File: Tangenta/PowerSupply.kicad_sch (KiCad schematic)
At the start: 64 parts, among them J1 39281243, U1 TPS54331DR, U2 TPS54331DR, U3 TPS54331DR, U4 TPS54331DR, U5 AMS1117-3_3, U6 AP7331-10WG-7

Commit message: AMS1117-3.3 and AP7331-10WG-7
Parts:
- U6: footprint AP7331-10WG:AP7331-10WG.kicad_sym -> CholaFootprintsPrjLib:AP7331-10WG.kicad_sym
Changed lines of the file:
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@@
       (effects (font (size 1.27 1.27)))
     )
-    (property "Footprint" "AP7331-10WG:AP7331-10WG.kicad_sym" (at 244.475 77.47 0)
+    (property "Footprint" "CholaFootprintsPrjLib:AP7331-10WG.kicad_sym" (at 244.475 77.47 0)
       (effects (font (size 1.27 1.27) italic) hide)
     )

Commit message: 24_Pin_Connector_Vertical
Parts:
- J1: footprint 24_Pin_Connector_Vertical:24_Pin_Connector_Vertical -> CholaFootprintsPrjLib:24_Pin_Connector_Vertical
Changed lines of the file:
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@@
       (effects (font (size 1.27 1.27)))
     )
-    (property "Footprint" "24_Pin_Connector_Vertical:24_Pin_Connector_Vertical" (at 191.135 158.496 0)
+    (property "Footprint" "CholaFootprintsPrjLib:24_Pin_Connector_Vertical" (at 191.135 158.496 0)
       (effects (font (size 1.27 1.27) italic) hide)
     )

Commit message: TPS54331DR
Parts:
- U1, U2, U3, U4: footprint TPS54331DR:TPS54331DR -> CholaFootprintsPrjLib:TPS54331DR
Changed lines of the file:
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@@
     )
   )
-  (symbol (lib_id "CholaSymbolsPrjLib:TPS54331DR") (at 85.725 71.12 0) (unit 1)
+  (symbol (lib_name "TPS54331DR_2") (lib_id "CholaSymbolsPrjLib:TPS54331DR") (at 85.725 71.12 0) (unit 1)
     (in_bom yes) (on_board yes) (dnp no) (fields_autoplaced)
     (property "Reference" "U2" (at 85.725 55.88 0)
@@
       (effects (font (size 1.27 1.27)))
     )
-    (property "Footprint" "TPS54331DR:TPS54331DR" (at 85.725 81.28 0)
+    (property "Footprint" "CholaFootprintsPrjLib:TPS54331DR" (at 85.725 81.28 0)
       (effects (font (size 1.27 1.27) italic) hide)
     )
@@
     )
   )
-  (symbol (lib_id "CholaSymbolsPrjLib:TPS54331DR") (at 85.725 111.125 0) (unit 1)
+  (symbol (lib_name "TPS54331DR_3") (lib_id "CholaSymbolsPrjLib:TPS54331DR") (at 85.725 111.125 0) (unit 1)
     (in_bom yes) (on_board yes) (dnp no) (fields_autoplaced)
     (property "Reference" "U3" (at 85.725 95.885 0)
@@
       (effects (font (size 1.27 1.27)))
     )
-    (property "Footprint" "TPS54331DR:TPS54331DR" (at 85.725 121.285 0)
+    (property "Footprint" "CholaFootprintsPrjLib:TPS54331DR" (at 85.725 121.285 0)
       (effects (font (size 1.27 1.27) italic) hide)
     )
@@
       (effects (font (size 1.27 1.27)))
     )
-    (property "Footprint" "TPS54331DR:TPS54331DR" (at 85.725 161.925 0)
+    (property "Footprint" "CholaFootprintsPrjLib:TPS54331DR" (at 85.725 161.925 0)
       (effects (font (size 1.27 1.27) italic) hide)
     )
@@
     )
   )
-  (symbol (lib_id "CholaSymbolsPrjLib:TPS54331DR") (at 85.725 31.75 0) (unit 1)
+  (symbol (lib_name "TPS54331DR_1") (lib_id "CholaSymbolsPrjLib:TPS54331DR") (at 85.725 31.75 0) (unit 1)
     (in_bom yes) (on_board yes) (dnp no) (fields_autoplaced)
     (property "Reference" "U1" (at 85.725 16.51 0)
@@
       (effects (font (size 1.27 1.27)))
     )
-    (property "Footprint" "TPS54331DR:TPS54331DR" (at 85.725 41.91 0)
-      (effects (font (size 1.27 1.27) italic) hide)
-    )
+    (property "Footprint" "CholaFootprintsPrjLib:TPS54331DR" (at 85.725 41.91 0)
+      (effects (font (size 1.27 1.27) italic) hide)
+    )

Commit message: B540C-13-F, CAP_L6
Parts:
- C2, C22, C23, C24, C25, C3, C4, C5: footprint CAP_L6:CAP_L6 -> CholaFootprintsPrjLib:CAP_L6
- D1, D2, D3, D4: footprint B540C-13-F:B540C-13-F -> CholaFootprintsPrjLib:B540C-13-F
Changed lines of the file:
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@@
       (effects (font (size 1.27 1.27)) (justify left))
     )
-    (property "Footprint" "CAP_L6:CAP_L6" (at 33.528 48.26 0)
+    (property "Footprint" "CholaFootprintsPrjLib:CAP_L6" (at 33.528 48.26 0)
       (effects (font (size 1.27 1.27) italic) hide)
     )
@@
     )
   )
-  (symbol (lib_id "CholaSymbolsPrjLib:35CE47AX") (at 30.48 108.585 0) (unit 1)
+  (symbol (lib_name "35CE47AX_6") (lib_id "CholaSymbolsPrjLib:35CE47AX") (at 30.48 108.585 0) (unit 1)
     (in_bom yes) (on_board yes) (dnp no)
     (property "Reference" "C4" (at 32.385 107.95 0)
@@
       (effects (font (size 1.27 1.27)) (justify left))
     )
-    (property "Footprint" "CAP_L6:CAP_L6" (at 33.528 127.635 0)
+    (property "Footprint" "CholaFootprintsPrjLib:CAP_L6" (at 33.528 127.635 0)
       (effects (font (size 1.27 1.27) italic) hide)
     )
@@
     )
   )
-  (symbol (lib_id "CholaSymbolsPrjLib:35CE47AX") (at 143.51 113.665 0) (unit 1)
+  (symbol (lib_name "35CE47AX_3") (lib_id "CholaSymbolsPrjLib:35CE47AX") (at 143.51 113.665 0) (unit 1)
     (in_bom yes) (on_board yes) (dnp no)
     (property "Reference" "C24" (at 145.415 113.665 0)
@@
       (effects (font (size 1.27 1.27)) (justify left))
     )
-    (property "Footprint" "CAP_L6:CAP_L6" (at 146.558 132.715 0)
+    (property "Footprint" "CholaFootprintsPrjLib:CAP_L6" (at 146.558 132.715 0)
       (effects (font (size 1.27 1.27) italic) hide)
     )
@@
     )
   )
-  (symbol (lib_id "CholaSymbolsPrjLib:B540C-13-F") (at 117.475 108.585 0) (unit 1)
+  (symbol (lib_name "B540C-13-F_3") (lib_id "CholaSymbolsPrjLib:B540C-13-F") (at 117.475 108.585 0) (unit 1)
     (in_bom yes) (on_board yes) (dnp no)
     (property "Reference" "D3" (at 116.205 106.045 0)
@@
       (effects (font (size 1.27 1.27)) (justify left) hide)
     )
-    (property "Footprint" "B540C-13-F:B540C-13-F" (at 117.602 120.142 0)
+    (property "Footprint" "CholaFootprintsPrjLib:B540C-13-F" (at 117.602 120.142 0)
       (effects (font (size 1.27 1.27) italic) hide)
     )
@@
     )
   )
-  (symbol (lib_id "CholaSymbolsPrjLib:35CE47AX") (at 30.48 149.225 0) (unit 1)
+  (symbol (lib_name "35CE47AX_5") (lib_id "CholaSymbolsPrjLib:35CE47AX") (at 30.48 149.225 0) (unit 1)
     (in_bom yes) (on_board yes) (dnp no)
     (property "Reference" "C5" (at 32.385 148.59 0)
@@
       (effects (font (size 1.27 1.27)) (justify left))
     )
-    (property "Footprint" "CAP_L6:CAP_L6" (at 33.528 168.275 0)
+    (property "Footprint" "CholaFootprintsPrjLib:CAP_L6" (at 33.528 168.275 0)
       (effects (font (size 1.27 1.27) italic) hide)
     )
@@
     )
   )
-  (symbol (lib_id "CholaSymbolsPrjLib:35CE47AX") (at 143.51 154.305 0) (unit 1)
+  (symbol (lib_name "35CE47AX_4") (lib_id "CholaSymbolsPrjLib:35CE47AX") (at 143.51 154.305 0) (unit 1)
     (in_bom yes) (on_board yes) (dnp no)
     (property "Reference" "C25" (at 145.415 154.305 0)
@@
       (effects (font (size 1.27 1.27)) (justify left))
     )
-    (property "Footprint" "CAP_L6:CAP_L6" (at 146.558 173.355 0)
+    (property "Footprint" "CholaFootprintsPrjLib:CAP_L6" (at 146.558 173.355 0)
       (effects (font (size 1.27 1.27) italic) hide)
     )
@@
     )
   )
-  (symbol (lib_id "CholaSymbolsPrjLib:B540C-13-F") (at 117.475 68.58 0) (unit 1)
+  (symbol (lib_name "B540C-13-F_2") (lib_id "CholaSymbolsPrjLib:B540C-13-F") (at 117.475 68.58 0) (unit 1)
     (in_bom yes) (on_board yes) (dnp no)
     (property "Reference" "D2" (at 116.205 66.04 0)
@@
       (effects (font (size 1.27 1.27)) (justify left) hide)
     )
-    (property "Footprint" "B540C-13-F:B540C-13-F" (at 117.602 80.137 0)
+    (property "Footprint" "CholaFootprintsPrjLib:B540C-13-F" (at 117.602 80.137 0)
       (effects (font (size 1.27 1.27) italic) hide)
     )
@@
       (effects (font (size 1.27 1.27)) (justify left) hide)
     )
-    (property "Footprint" "B540C-13-F:B540C-13-F" (at 117.602 160.782 0)
+    (property "Footprint" "CholaFootprintsPrjLib:B540C-13-F" (at 117.602 160.782 0)
       (effects (font (size 1.27 1.27) italic) hide)
     )
@@
     )
   )
-  (symbol (lib_id "CholaSymbolsPrjLib:B540C-13-F") (at 117.475 29.21 0) (unit 1)
+  (symbol (lib_name "B540C-13-F_1") (lib_id "CholaSymbolsPrjLib:B540C-13-F") (at 117.475 29.21 0) (unit 1)
     (in_bom yes) (on_board yes) (dnp no)
     (property "Reference" "D1" (at 116.205 26.67 0)
@@
       (effects (font (size 1.27 1.27)) (justify left) hide)
     )
-    (property "Footprint" "B540C-13-F:B540C-13-F" (at 117.602 40.767 0)
+    (property "Footprint" "CholaFootprintsPrjLib:B540C-13-F" (at 117.602 40.767 0)
       (effects (font (size 1.27 1.27) italic) hide)
     )
@@
     )
   )
-  (symbol (lib_id "CholaSymbolsPrjLib:35CE47AX") (at 143.51 73.66 0) (unit 1)
+  (symbol (lib_name "35CE47AX_2") (lib_id "CholaSymbolsPrjLib:35CE47AX") (at 143.51 73.66 0) (unit 1)
     (in_bom yes) (on_board yes) (dnp no)
     (property "Reference" "C23" (at 145.415 73.66 0)
@@
       (effects (font (size 1.27 1.27)) (justify left))
     )
-    (property "Footprint" "CAP_L6:CAP_L6" (at 146.558 92.71 0)
+    (property "Footprint" "CholaFootprintsPrjLib:CAP_L6" (at 146.558 92.71 0)
       (effects (font (size 1.27 1.27) italic) hide)
     )
@@
     )
   )
-  (symbol (lib_id "CholaSymbolsPrjLib:35CE47AX") (at 143.51 34.29 0) (unit 1)
+  (symbol (lib_name "35CE47AX_1") (lib_id "CholaSymbolsPrjLib:35CE47AX") (at 143.51 34.29 0) (unit 1)
     (in_bom yes) (on_board yes) (dnp no)
     (property "Reference" "C22" (at 145.415 34.29 0)
@@
       (effects (font (size 1.27 1.27)) (justify left))
     )
-    (property "Footprint" "CAP_L6:CAP_L6" (at 146.558 53.34 0)
+    (property "Footprint" "CholaFootprintsPrjLib:CAP_L6" (at 146.558 53.34 0)
       (effects (font (size 1.27 1.27) italic) hide)
     )
@@
     )
   )
-  (symbol (lib_id "CholaSymbolsPrjLib:35CE47AX") (at 30.48 68.58 0) (unit 1)
+  (symbol (lib_name "35CE47AX_7") (lib_id "CholaSymbolsPrjLib:35CE47AX") (at 30.48 68.58 0) (unit 1)
     (in_bom yes) (on_board yes) (dnp no)
     (property "Reference" "C3" (at 32.385 67.945 0)
@@
       (effects (font (size 1.27 1.27)) (justify left))
     )
-    (property "Footprint" "CAP_L6:CAP_L6" (at 33.528 87.63 0)
-      (effects (font (size 1.27 1.27) italic) hide)
-    )
+    (property "Footprint" "CholaFootprintsPrjLib:CAP_L6" (at 33.528 87.63 0)
+      (effects (font (size 1.27 1.27) italic) hide)
+    )

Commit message: SLO0650H6Р8МТТ, CAP_TANTAL_A
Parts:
- C26, C27, C28, C29, C32: footprint CAP_TANTAL_A:CAP_TANTAL_A -> CholaFootprintsPrjLib:CAP_TANTAL_A
- L1, L2, L3, L4: footprint Choke:Choke -> CholaFootprintsPrjLib:Choke
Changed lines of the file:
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@@
       (effects (font (size 1.27 1.27)))
     )
-    (property "Footprint" "Choke:Choke" (at 120.015 132.334 0)
+    (property "Footprint" "CholaFootprintsPrjLib:Choke" (at 120.015 132.334 0)
       (effects (font (size 1.27 1.27) italic) hide)
     )
@@
       (effects (font (size 1.27 1.27)) (justify right))
     )
-    (property "Footprint" "CAP_TANTAL_A:CAP_TANTAL_A" (at 140.081 110.617 0)
+    (property "Footprint" "CholaFootprintsPrjLib:CAP_TANTAL_A" (at 140.081 110.617 0)
       (effects (font (size 1.27 1.27) italic) hide)
     )
@@
       (effects (font (size 1.27 1.27)) (justify right))
     )
-    (property "Footprint" "CAP_TANTAL_A:CAP_TANTAL_A" (at 140.081 31.242 0)
+    (property "Footprint" "CholaFootprintsPrjLib:CAP_TANTAL_A" (at 140.081 31.242 0)
       (effects (font (size 1.27 1.27) italic) hide)
     )
@@
       (effects (font (size 1.27 1.27)))
     )
-    (property "Footprint" "Choke:Choke" (at 120.015 12.319 0)
+    (property "Footprint" "CholaFootprintsPrjLib:Choke" (at 120.015 12.319 0)
       (effects (font (size 1.27 1.27) italic) hide)
     )
@@
       (effects (font (size 1.27 1.27)))
     )
-    (property "Footprint" "Choke:Choke" (at 120.015 51.689 0)
+    (property "Footprint" "CholaFootprintsPrjLib:Choke" (at 120.015 51.689 0)
       (effects (font (size 1.27 1.27) italic) hide)
     )
@@
       (effects (font (size 1.27 1.27)) (justify right))
     )
-    (property "Footprint" "CAP_TANTAL_A:CAP_TANTAL_A" (at 241.681 33.782 0)
+    (property "Footprint" "CholaFootprintsPrjLib:CAP_TANTAL_A" (at 241.681 33.782 0)
       (effects (font (size 1.27 1.27) italic) hide)
     )
@@
       (effects (font (size 1.27 1.27)) (justify right))
     )
-    (property "Footprint" "CAP_TANTAL_A:CAP_TANTAL_A" (at 140.081 70.612 0)
+    (property "Footprint" "CholaFootprintsPrjLib:CAP_TANTAL_A" (at 140.081 70.612 0)
       (effects (font (size 1.27 1.27) italic) hide)
     )
@@
       (effects (font (size 1.27 1.27)))
     )
-    (property "Footprint" "Choke:Choke" (at 120.015 91.694 0)
+    (property "Footprint" "CholaFootprintsPrjLib:Choke" (at 120.015 91.694 0)
       (effects (font (size 1.27 1.27) italic) hide)
     )
@@
       (effects (font (size 1.27 1.27)) (justify right))
     )
-    (property "Footprint" "CAP_TANTAL_A:CAP_TANTAL_A" (at 140.081 151.257 0)
-      (effects (font (size 1.27 1.27) italic) hide)
-    )
+    (property "Footprint" "CholaFootprintsPrjLib:CAP_TANTAL_A" (at 140.081 151.257 0)
+      (effects (font (size 1.27 1.27) italic) hide)
+    )

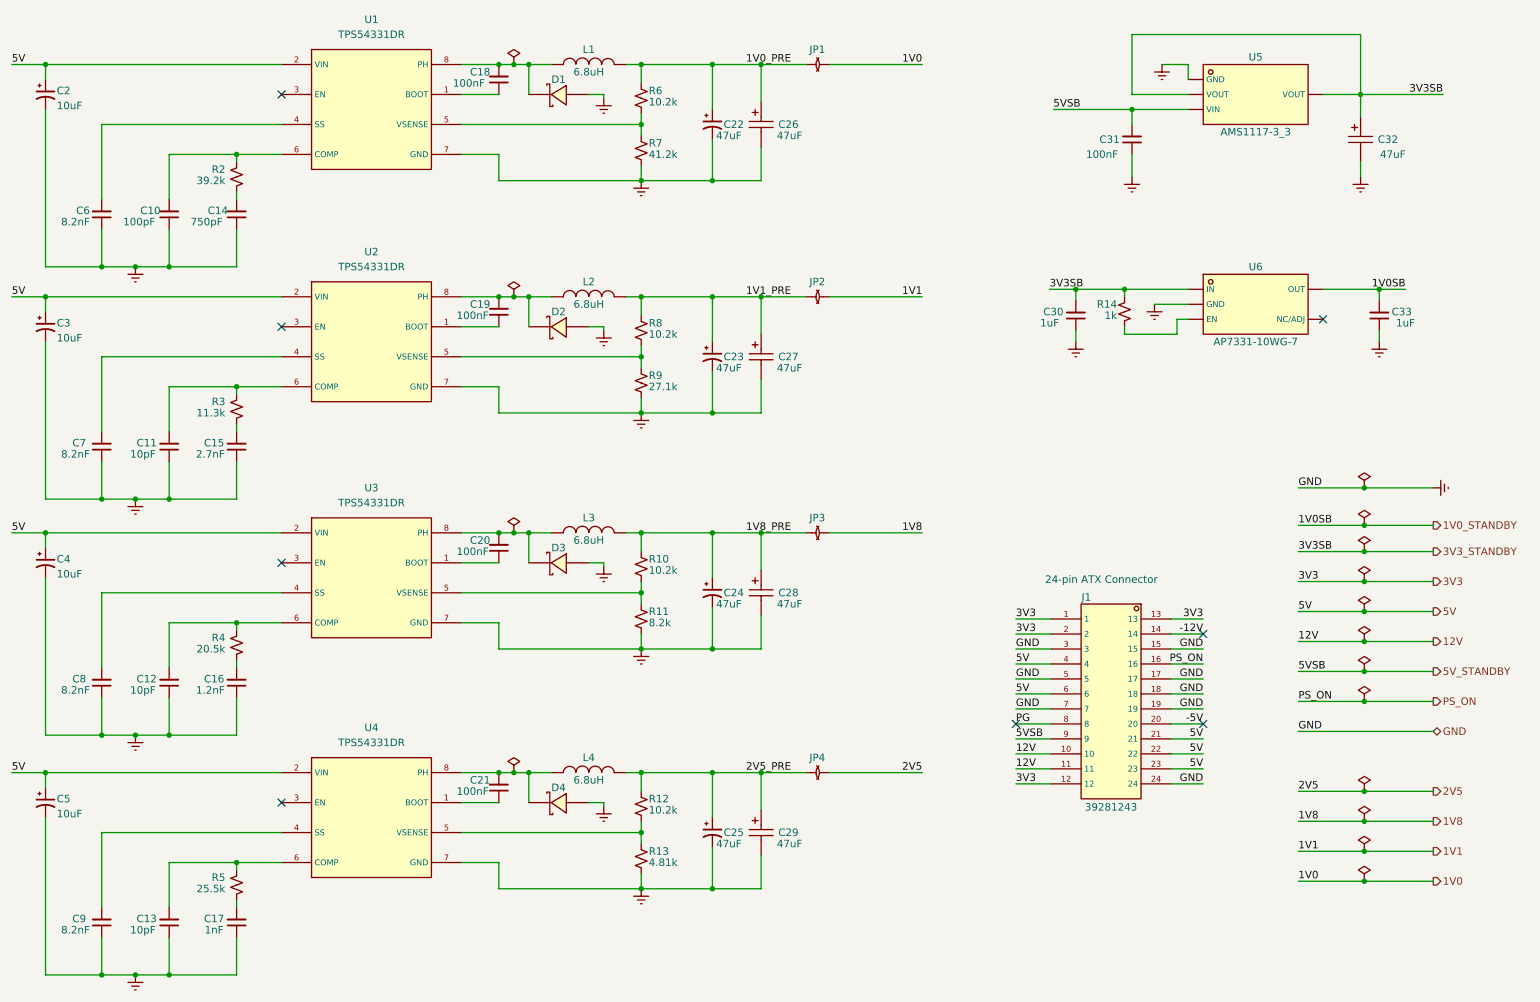
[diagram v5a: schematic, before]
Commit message: Saved in KiCAD9, ERC and DRC pass.
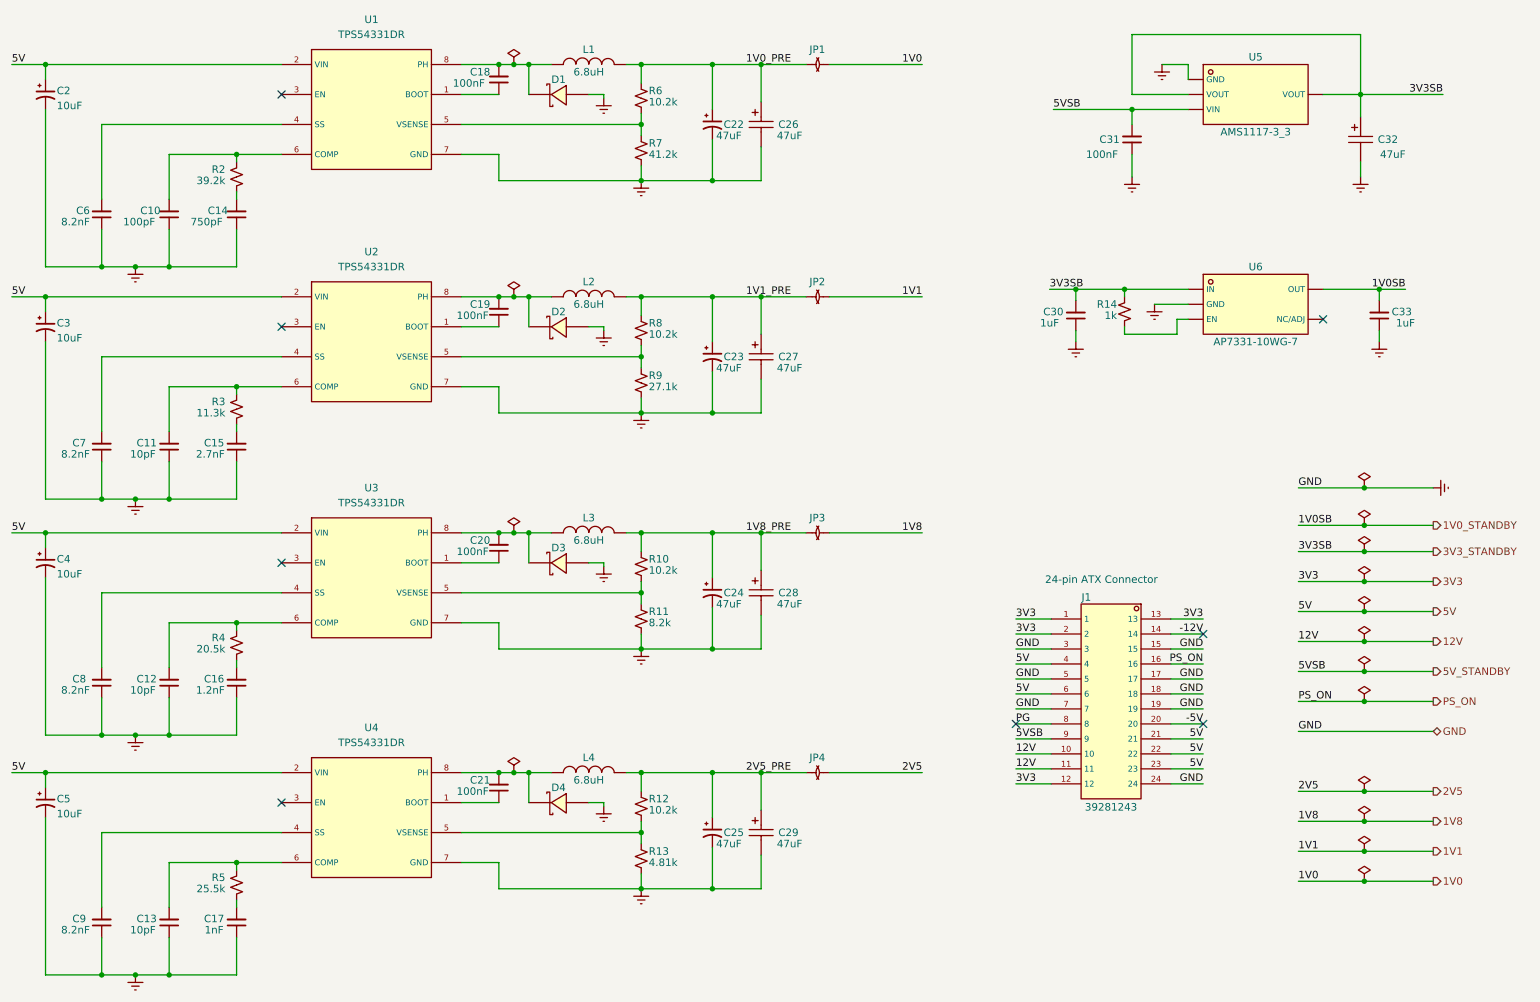
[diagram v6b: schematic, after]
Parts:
- U1: footprint CholaFootprintsPrjLib:TPS54331DR -> TPS54331DR:TPS54331DR

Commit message: Moving the TPS from the local to the global lib.
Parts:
- U1: symbol CholaSymbolsPrjLib:TPS54331DR -> TPS54331DR:TPS54331DR
- U2, U3, U4: footprint CholaFootprintsPrjLib:TPS54331DR -> TPS54331DR:TPS54331DR; symbol CholaSymbolsPrjLib:TPS54331DR -> TPS54331DR:TPS54331DR
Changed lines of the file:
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@@
 	(symbol
 		(lib_name "TPS54331DR_2")
-		(lib_id "CholaSymbolsPrjLib:TPS54331DR")
+		(lib_id "TPS54331DR:TPS54331DR")
 		(at 85.725 71.12 0)
 		(unit 1)
@@
 			)
 		)
-		(property "Footprint" "CholaFootprintsPrjLib:TPS54331DR"
+		(property "Footprint" "TPS54331DR:TPS54331DR"
 			(at 85.725 81.28 0)
 			(effects
@@
 	(symbol
 		(lib_name "TPS54331DR_3")
-		(lib_id "CholaSymbolsPrjLib:TPS54331DR")
+		(lib_id "TPS54331DR:TPS54331DR")
 		(at 85.725 111.125 0)
 		(unit 1)
@@
 			)
 		)
-		(property "Footprint" "CholaFootprintsPrjLib:TPS54331DR"
+		(property "Footprint" "TPS54331DR:TPS54331DR"
 			(at 85.725 121.285 0)
 			(effects
@@
 	)
 	(symbol
-		(lib_id "CholaSymbolsPrjLib:TPS54331DR")
+		(lib_id "TPS54331DR:TPS54331DR")
 		(at 85.725 151.765 0)
 		(unit 1)
@@
 			)
 		)
-		(property "Footprint" "CholaFootprintsPrjLib:TPS54331DR"
+		(property "Footprint" "TPS54331DR:TPS54331DR"
 			(at 85.725 161.925 0)
 			(effects
@@
 	(symbol
 		(lib_name "TPS54331DR_1")
-		(lib_id "CholaSymbolsPrjLib:TPS54331DR")
+		(lib_id "TPS54331DR:TPS54331DR")
 		(at 85.725 31.75 0)
 		(unit 1)

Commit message: Removing component association with previous project (local) libraries.
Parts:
- C10, C11, C12, C13, C14, C15, C16, C17, C18, C19, C20, C21, C30, C31, C33, C6, C7, C8, C9: symbol CholaSymbolsPrjLib:C_Small -> C_Small:C_Small
- C2, C22, C23, C24, C25, C3, C4, C5: footprint CholaFootprintsPrjLib:CAP_L6 -> CAP_L6:CAP_L6; symbol CholaSymbolsPrjLib:35CE47AX -> 35CE47AX:35CE47AX
- C26, C27, C28, C29, C32: footprint CholaFootprintsPrjLib:CAP_TANTAL_A -> CAP_TANTAL_A:CAP_TANTAL_A; symbol CholaSymbolsPrjLib:CA45-A-6_3V-47UF-K -> CA45-A-6_3V-47UF-K:CA45-A-6_3V-47UF-K
- D1, D2, D3, D4: footprint CholaFootprintsPrjLib:B540C-13-F -> B540C-13-F:B540C-13-F; symbol CholaSymbolsPrjLib:B540C-13-F -> B540C-13-F:B540C-13-F
- J1: footprint CholaFootprintsPrjLib:24_Pin_Connector_Vertical -> 24_Pin_Connector_Vertical:24_Pin_Connector_Vertical; symbol CholaSymbolsPrjLib:39281243 -> 39281243:39281243
- JP1, JP2, JP3, JP4: symbol CholaSymbolsPrjLib:CustomJumper -> CustomJumper:CustomJumper
- L1, L2, L3, L4: footprint CholaFootprintsPrjLib:Choke -> Choke:Choke; symbol CholaSymbolsPrjLib:SLO0650H6R8MTT -> SLO0650H6R8MTT:SLO0650H6R8MTT
- R10, R11, R12, R13, R14, R2, R3, R4, R5, R6, R7, R8, R9: symbol CholaSymbolsPrjLib:R_Small_US -> R_Small_US:R_Small_US
- U5: footprint CholaFootprintsPrjLib:AMS1117-3.3 -> AMS1117-3.3:AMS1117-3.3; symbol CholaSymbolsPrjLib:AMS1117-3_3 -> AMS1117-3_3:AMS1117-3_3
- U6: footprint CholaFootprintsPrjLib:AP7331-10WG.kicad_sym -> AP7331-10WG.kicad_sym:AP7331-10WG.kicad_sym; symbol CholaSymbolsPrjLib:AP7331-10WG-7 -> AP7331-10WG-7:AP7331-10WG-7
